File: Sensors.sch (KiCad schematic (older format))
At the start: 21 parts, among them U1 MCP60x4, U2 HTU21D, U3 PIR

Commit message: Finish schematic, assign all footprints for V3
Signed-off-by: pluyckx <philip.luyckx@gmail.com>
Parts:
- C10, C8, C9: footprint (none) -> Resistors_SMD:R_0805
- U1: footprint (none) -> CustomSmd:SOIC-14
- U2: footprint (none) -> CustomSmd:HTU21D_QFN
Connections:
- net +BATT is gone; now on net +1V8: C9.1, U2.5 (VDD)
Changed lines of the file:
@@
 encoding utf-8
 Sheet 5 6
-Title ""
-Date ""
-Rev ""
-Comp ""
+Title "Sensor"
+Date "2016-06-05"
+Rev "3"
+Comp "Philip Luyckx"
 Comment1 ""
 Comment2 ""
@@
 	650  2200 650  800
 $Comp
-L +BATT #PWR027
-U 1 1 5753530B
-P 1500 3900
-F 0 "#PWR027" H 1500 3750 50  0001 C CNN
-F 1 "+BATT" H 1500 4040 50  0000 C CNN
-F 2 "" H 1500 3900 50  0000 C CNN
-F 3 "" H 1500 3900 50  0000 C CNN
-	1    1500 3900
-	1    0    0    -1
-$EndComp
-$Comp
 L HTU21D U2
 U 1 1 575356C5
@@
 F 0 "U2" H 1950 3350 60  0000 C CNN
 F 1 "HTU21D" H 1950 3850 60  0000 C CNN
-F 2 "" H 1950 3800 60  0000 C CNN
+F 2 "CustomSmd:HTU21D_QFN" H 1950 3800 60  0001 C CNN
 F 3 "" H 1950 3800 60  0000 C CNN
 	1    1950 3800
@@
 $EndComp
 $Comp
-L GND #PWR028
+L GND #PWR027
 U 1 1 57535772
 P 1500 4100
-F 0 "#PWR028" H 1500 3850 50  0001 C CNN
+F 0 "#PWR027" H 1500 3850 50  0001 C CNN
 F 1 "GND" H 1500 3950 50  0000 C CNN
 F 2 "" H 1500 4100 50  0000 C CNN
@@
 F 0 "C9" H 1275 4100 50  0000 L CNN
 F 1 "100nF" H 900 4000 50  0000 L CNN
-F 2 "" H 1288 3850 50  0000 C CNN
+F 2 "Resistors_SMD:R_0805" H 1288 3850 50  0001 C CNN
 F 3 "" H 1250 4000 50  0000 C CNN
 	1    1250 4000
@@
 F 0 "U1" H 2750 750 60  0000 C CNN
 F 1 "MCP60x4" H 2850 1150 60  0000 C CNN
-F 2 "" H 2650 1150 60  0000 C CNN
+F 2 "CustomSmd:SOIC-14" H 2650 1150 60  0001 C CNN
 F 3 "" H 2650 1150 60  0000 C CNN
 	4    2650 1150
@@
 F 0 "U1" H 6350 3550 60  0000 C CNN
 F 1 "MCP60x4" H 6450 3950 60  0000 C CNN
-F 2 "" H 6250 3950 60  0000 C CNN
+F 2 "CustomSmd:SOIC-14" H 6250 3950 60  0001 C CNN
 F 3 "" H 6250 3950 60  0000 C CNN
 	2    6250 3950
@@
 F 0 "U1" H 7950 3450 60  0000 C CNN
 F 1 "MCP60x4" H 8050 3850 60  0000 C CNN
-F 2 "" H 7850 3850 60  0000 C CNN
+F 2 "CustomSmd:SOIC-14" H 7850 3850 60  0001 C CNN
 F 3 "" H 7850 3850 60  0000 C CNN
 	1    7850 3850
@@
 F 0 "U1" H 3800 5050 60  0000 C CNN
 F 1 "MCP60x4" H 3900 5450 60  0000 C CNN
-F 2 "" H 3700 5450 60  0000 C CNN
+F 2 "CustomSmd:SOIC-14" H 3700 5450 60  0001 C CNN
 F 3 "" H 3700 5450 60  0000 C CNN
 	3    3700 5450
@@
 F 0 "U1" H 2000 5150 60  0000 C CNN
 F 1 "MCP60x4" H 2100 5550 60  0000 C CNN
-F 2 "" H 1900 5550 60  0000 C CNN
+F 2 "CustomSmd:SOIC-14" H 1900 5550 60  0001 C CNN
 F 3 "" H 1900 5550 60  0000 C CNN
 	5    1900 5550
@@
 $EndComp
 $Comp
-L +1V8 #PWR029
+L +1V8 #PWR028
 U 1 1 57539252
 P 1850 5400
-F 0 "#PWR029" H 1850 5250 50  0001 C CNN
+F 0 "#PWR028" H 1850 5250 50  0001 C CNN
 F 1 "+1V8" H 1850 5540 50  0000 C CNN
 F 2 "" H 1850 5400 50  0000 C CNN
@@
 $EndComp
 $Comp
-L GND #PWR030
+L GND #PWR029
 U 1 1 5753929C
 P 1850 6100
-F 0 "#PWR030" H 1850 5850 50  0001 C CNN
+F 0 "#PWR029" H 1850 5850 50  0001 C CNN
 F 1 "GND" H 1850 5950 50  0000 C CNN
 F 2 "" H 1850 6100 50  0000 C CNN
@@
 F 0 "C10" H 1425 5850 50  0000 L CNN
 F 1 "100nF" H 1425 5650 50  0000 L CNN
-F 2 "" H 1438 5600 50  0000 C CNN
+F 2 "Resistors_SMD:R_0805" H 1438 5600 50  0001 C CNN
 F 3 "" H 1400 5750 50  0000 C CNN
 	1    1400 5750
@@
 F 0 "C8" H 1175 5850 50  0000 L CNN
 F 1 "1uF" H 1175 5650 50  0000 L CNN
-F 2 "" H 1188 5600 50  0000 C CNN
+F 2 "Resistors_SMD:R_0805" H 1188 5600 50  0001 C CNN
 F 3 "" H 1150 5750 50  0000 C CNN
 	1    1150 5750
@@
 Wire Wire Line
 	7250 2650 7250 2750
+$Comp
+L +1V8 #PWR030
+U 1 1 575B235E
+P 1500 3900
+F 0 "#PWR030" H 1500 3750 50  0001 C CNN
+F 1 "+1V8" H 1500 4040 50  0000 C CNN
+F 2 "" H 1500 3900 50  0000 C CNN
+F 3 "" H 1500 3900 50  0000 C CNN
+	1    1500 3900
+	1    0    0    -1
+$EndComp
 $EndSCHEMATC

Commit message: Finish routing v4
Signed-off-by: pluyckx <philip.luyckx@gmail.com>
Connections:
- net ADC_Light: now also U1.8; no longer U1.14
- net GND: now also U1.10 (+); no longer U1.12 (+)
- net Motion_Offset: now also U1.12 (+); no longer U1.10 (+)
- net at D2.1, R5.2: now also U1.9 (-); no longer U1.13 (-)
- new net: U1.13 (-), U1.14
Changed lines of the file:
@@
 $Comp
 L MCP60x4 U1
-U 4 1 57538AEE
+U 3 1 57538AEE
 P 2650 1150
 F 0 "U1" H 2750 750 60  0000 C CNN
@@
 F 2 "CustomSmd:SOIC-14" H 2650 1150 60  0001 C CNN
 F 3 "" H 2650 1150 60  0000 C CNN
-	4    2650 1150
+	3    2650 1150
 	1    0    0    -1
 $EndComp
@@
 $Comp
 L MCP60x4 U1
-U 3 1 57538FA3
+U 4 1 57538FA3
 P 3700 5450
 F 0 "U1" H 3800 5050 60  0000 C CNN
@@
 F 2 "CustomSmd:SOIC-14" H 3700 5450 60  0001 C CNN
 F 3 "" H 3700 5450 60  0000 C CNN
-	3    3700 5450
+	4    3700 5450
 	1    0    0    -1
 $EndComp

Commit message: Update some routing
Signed-off-by: pluyckx <philip.luyckx@gmail.com>
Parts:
- added R15, R16: 1M, Resistors_SMD:R_0603, symbol R
- added R17: 1.6M, Resistors_SMD:R_0603, symbol R
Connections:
- net +1V8: now also R15.1
- net ADC_Motion: now also U1.13 (-)
- net GND: now also R16.2
- net Motion_Offset: no longer U1.12 (+)
- net DIG_Motion: now reaches U1.14
- net DIG_Motion: now also R17.1; no longer U1.13 (-)
- new net: R15.2, R16.1, R17.2, U1.12 (+)
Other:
- note removed: "Unused opamp"
- moved on the sheet: U1D
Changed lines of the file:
@@
 Wire Wire Line
 	8300 4800 8300 4050
-Wire Wire Line
-	8200 4050 8650 4050
 Connection ~ 8000 4800
 Wire Wire Line
@@
 Connection ~ 6700 4150
 Connection ~ 8300 4050
-Text GLabel 8650 4050 2    60   Output ~ 0
+Text GLabel 8550 4050 2    60   Output ~ 0
 ADC_Motion
 Text Notes 5050 6100 0    60   ~ 0
@@
 Text Notes 850  3650 0    60   ~ 0
 Temperature & Humidity sensor
-Wire Wire Line
-	3450 5750 3450 5950
-Wire Wire Line
-	3450 5950 4050 5950
 $Comp
 L MCP60x4 U1
@@
 L MCP60x4 U1
 U 4 1 57538FA3
-P 3700 5450
-F 0 "U1" H 3800 5050 60  0000 C CNN
-F 1 "MCP60x4" H 3900 5450 60  0000 C CNN
-F 2 "CustomSmd:SOIC-14" H 3700 5450 60  0001 C CNN
-F 3 "" H 3700 5450 60  0000 C CNN
-	4    3700 5450
+P 10300 3950
+F 0 "U1" H 10400 3550 60  0000 C CNN
+F 1 "MCP60x4" H 10500 3950 60  0000 C CNN
+F 2 "CustomSmd:SOIC-14" H 10300 3950 60  0001 C CNN
+F 3 "" H 10300 3950 60  0000 C CNN
+	4    10300 3950
 	1    0    0    -1
 $EndComp
@@
 Wire Wire Line
 	1300 5400 1850 5400
-Wire Wire Line
-	4050 5950 4050 5650
-Text GLabel 3450 5550 0    60   Input ~ 0
-Motion_Offset
 Wire Notes Line
 	1000 5150 2400 5150
@@
 Wire Notes Line
 	1000 6350 1000 5150
-Wire Notes Line
-	2650 5150 4200 5150
-Wire Notes Line
-	4200 5150 4200 6350
-Wire Notes Line
-	4200 6350 2650 6350
-Wire Notes Line
-	2650 6350 2650 5150
 Text Notes 1000 5150 0    60   ~ 0
 Opamp supply
-Text Notes 2650 5150 0    60   ~ 0
-Unused opamp
 Wire Wire Line
 	7250 2650 7250 2750
@@
 	1    0    0    -1
 $EndComp
+Text GLabel 10050 4250 0    60   Input ~ 0
+ADC_Motion
+$Comp
+L R R15
+U 1 1 57802832
+P 9400 3800
+F 0 "R15" V 9480 3800 50  0000 C CNN
+F 1 "1M" V 9400 3800 50  0000 C CNN
+F 2 "Resistors_SMD:R_0603" V 9330 3800 50  0001 C CNN
+F 3 "" H 9400 3800 50  0000 C CNN
+	1    9400 3800
+	1    0    0    -1
+$EndComp
+$Comp
+L R R16
+U 1 1 578028BF
+P 9400 4300
+F 0 "R16" V 9480 4300 50  0000 C CNN
+F 1 "1M" V 9400 4300 50  0000 C CNN
+F 2 "Resistors_SMD:R_0603" V 9330 4300 50  0001 C CNN
+F 3 "" H 9400 4300 50  0000 C CNN
+	1    9400 4300
+	1    0    0    -1
+$EndComp
+$Comp
+L +1V8 #PWR031
+U 1 1 5780291A
+P 9400 3650
+F 0 "#PWR031" H 9400 3500 50  0001 C CNN
+F 1 "+1V8" H 9400 3790 50  0000 C CNN
+F 2 "" H 9400 3650 50  0000 C CNN
+F 3 "" H 9400 3650 50  0000 C CNN
+	1    9400 3650
+	1    0    0    -1
+$EndComp
+Wire Wire Line
+	9400 3950 9400 4150
+$Comp
+L GND #PWR032
+U 1 1 578029DA
+P 9400 4450
+F 0 "#PWR032" H 9400 4200 50  0001 C CNN
+F 1 "GND" H 9400 4300 50  0000 C CNN
+F 2 "" H 9400 4450 50  0000 C CNN
+F 3 "" H 9400 4450 50  0000 C CNN
+	1    9400 4450
+	1    0    0    -1
+$EndComp
+Wire Wire Line
+	9400 4050 10050 4050
+Connection ~ 9400 4050
+Wire Wire Line
+	10050 4050 10050 3750
+Wire Wire Line
+	10050 3750 10150 3750
+$Comp
+L R R17
+U 1 1 57802B72
+P 10300 3750
+F 0 "R17" V 10380 3750 50  0000 C CNN
+F 1 "1.6M" V 10300 3750 50  0000 C CNN
+F 2 "Resistors_SMD:R_0603" V 10230 3750 50  0001 C CNN
+F 3 "" H 10300 3750 50  0000 C CNN
+	1    10300 3750
+	0    1    1    0
+$EndComp
+Wire Wire Line
+	10450 3750 10650 3750
+Wire Wire Line
+	10650 3750 10650 4150
+Text GLabel 10650 4150 2    60   Output ~ 0
+DIG_Motion
+Wire Wire Line
+	8200 4050 8550 4050
 $EndSCHEMATC

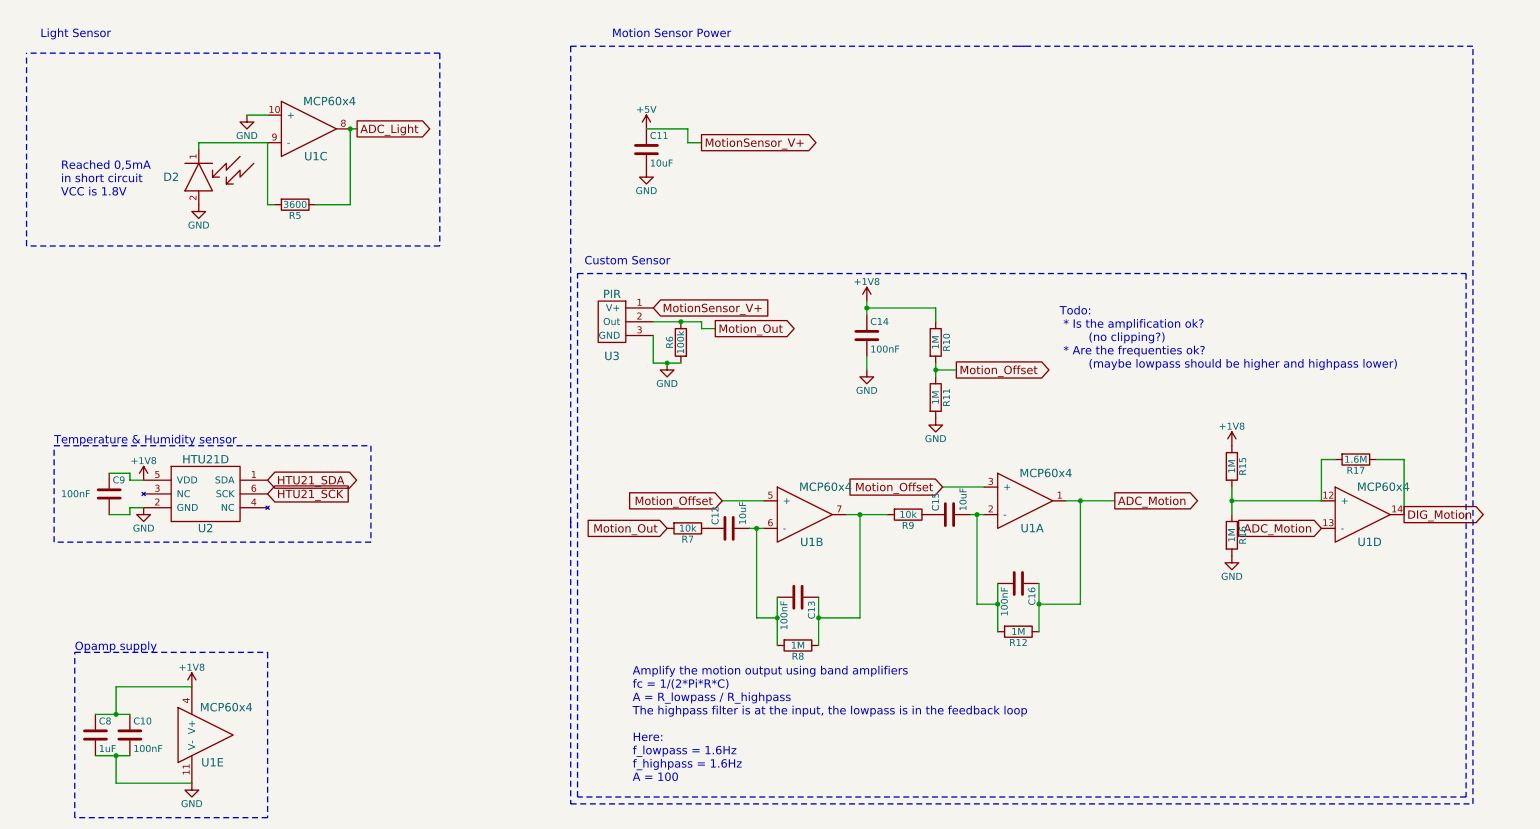
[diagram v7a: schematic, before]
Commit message: Corrections I2C and Dig Opamp out
 * Fix level shift for I2C
 * Fix level shift opamp digital out (PIR)

Signed-off-by: Philip Luyckx <philip.luyckx@gmail.com>
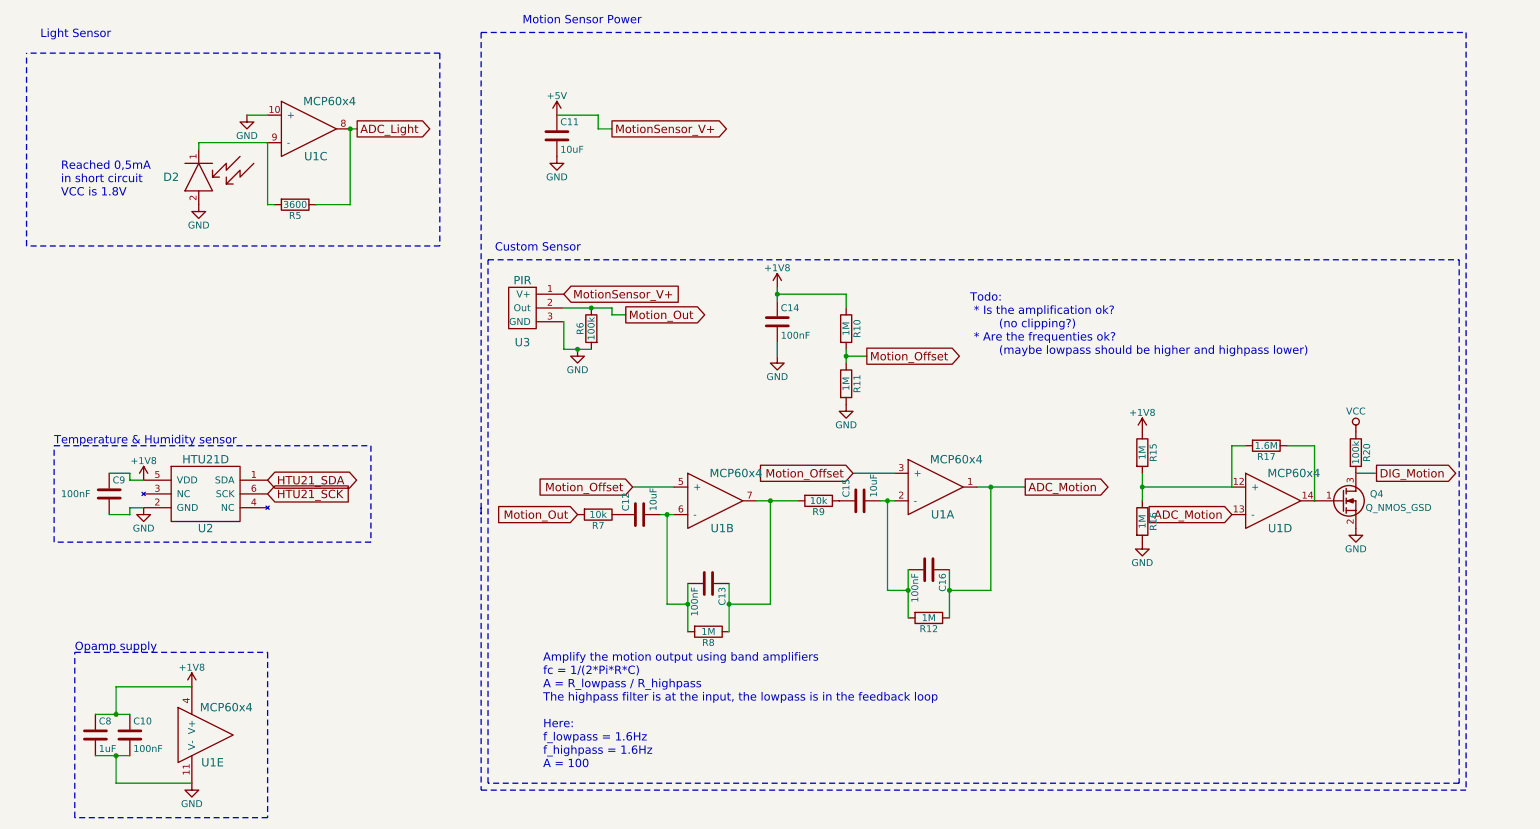
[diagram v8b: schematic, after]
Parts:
- added Q4: Q_NMOS_GSD, CustomSmd:SOT23, symbol Q_NMOS_GSD
- added R20: 100k, Resistors_SMD:R_0603, symbol R
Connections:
- net DIG_Motion: now also Q4.3 (D), R20.2; no longer R17.1, U1.14
- net GND: now also Q4.2 (S)
- new net: Q4.1 (G), R17.1, U1.14
- new net VCC: R20.1
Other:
- moved on the sheet: C11, C12, C13, C14, C15, C16, R10, R11, R12, R15, R16, R17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
